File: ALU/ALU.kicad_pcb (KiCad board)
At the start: 4 copper layers, 100 x 100 mm, 78 parts, among them IC1 SN74AHCT16245DGGR, J1 Conn_01x06_Pin, J2 Conn_02x15_Odd_Even, J3 Conn_02x15_Odd_Even, J4 Conn_02x15_Odd_Even, J5 Conn_01x01_Pin, J6 Conn_01x01_Pin, J7 Conn_01x01_Pin, J8 Conn_01x01_Pin, J9 Conn_01x02, U1 74AHC1G08, U10 74HCT21, U11 74AHC1G32DBVR, U12 74AHCT1G02DBVR, U13 74AHCT1G08DBVR, U14 74AHCT1G08DBVR, U15 74AHC1G32DBVR, U16 74AHC1G32DBVR, U17 74AHC1G08, U18 SN74AHCT16374DGGR, U19 74AHCT1G08DBVR, U2 SN74AHCT16374DGGR, U20 74AHCT1G02DBVR, U21 74AHCT1G02DBVR, U3 74AHC1G04DBVR, U4 74LS181, U5 74LS181, U6 74AHCT1G08DBVR, U7 74HCT11, U8 74LS181, U9 74LS181

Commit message: Started GPU
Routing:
- net GND: track 156.3 -> 159.2 mm, vias 41 -> 47
- net /INA/DIN2: track 13.1 -> 13.8 mm
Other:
- outline, holes or cut-outs redrawn

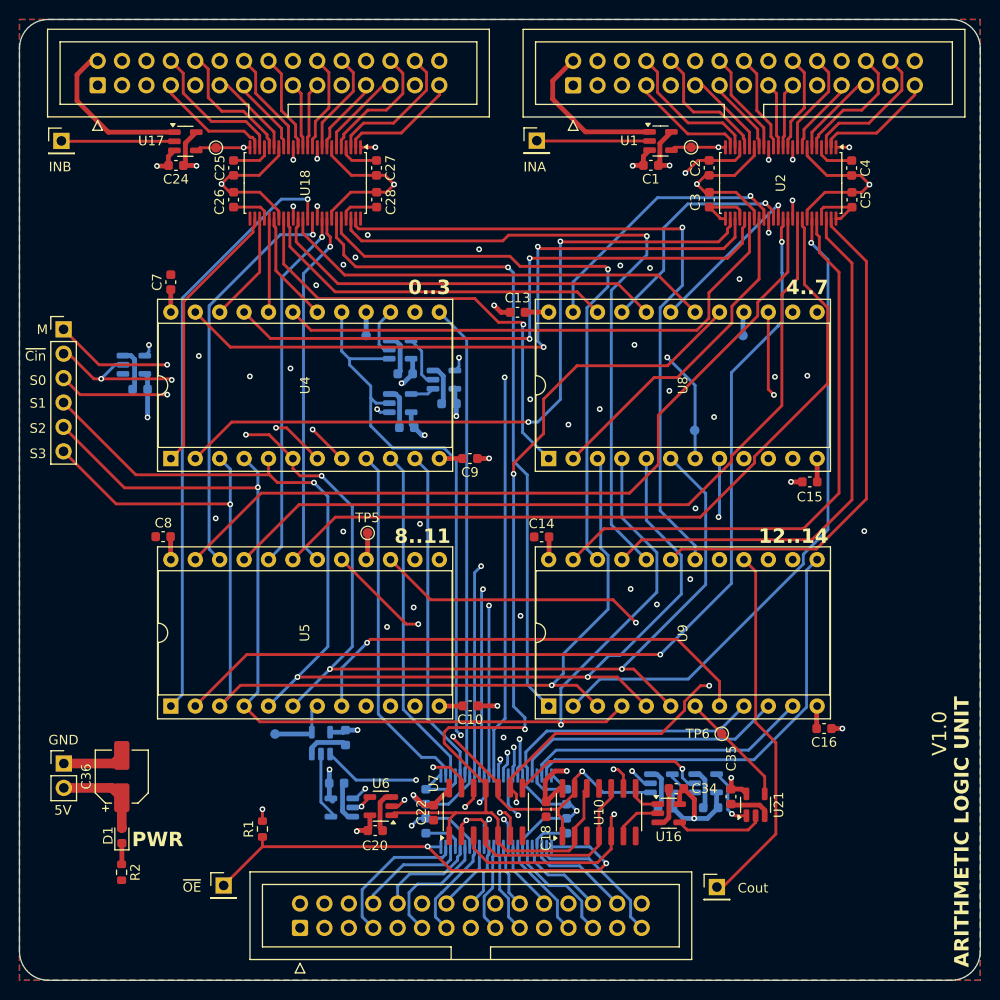
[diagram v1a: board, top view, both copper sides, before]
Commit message: Fixed incorrect wiring in ALU (input registers)
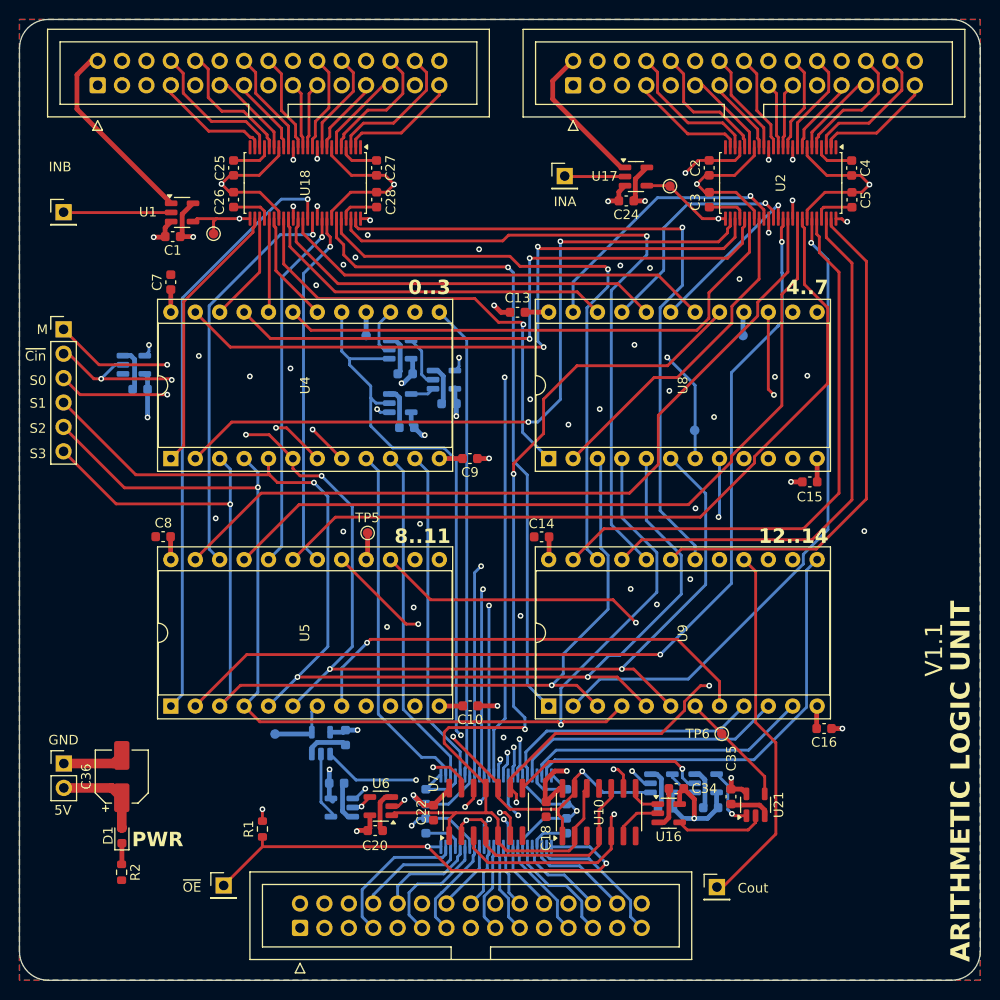
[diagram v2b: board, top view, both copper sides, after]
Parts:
- moved TP2 8.95 mm to (154.2, 36.3)
- moved J6 7.42 mm to (138.6, 34.1)
- moved C1 7.41 mm to (150.0, 36.6)
- moved U1 7.41 mm to (150.9, 34.1)
- moved J5 4.70 mm to (190.8, 30.3)
- moved TP1 4.61 mm to (201.7, 31.4)
- moved U17 4.50 mm to (198.2, 30.4)
- moved C24 4.50 mm to (197.2, 32.9)
- renumbered C24 to C1, C1 to C24, U17 to U1, U1 to U17
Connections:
- TP1 pad 1: Net-(U2-1~{OE}) -> Net-(U2-1CLK)
- TP2 pad 1: Net-(U18-1~{OE}) -> Net-(U18-1CLK)
- U1 pad 4: Net-(U18-1~{OE}) -> Net-(U18-1CLK)
- U17 pad 4: Net-(U2-1~{OE}) -> Net-(U2-1CLK)
- U18 pad 1: Net-(U18-1~{OE}) -> GND
- U18 pad 24: Net-(U18-1~{OE}) -> GND
- U18 pad 25: GND -> Net-(U18-1CLK)
- U18 pad 48: GND -> Net-(U18-1CLK)
- U2 pad 1: Net-(U2-1~{OE}) -> GND
- U2 pad 24: Net-(U2-1~{OE}) -> GND
- U2 pad 25: GND -> Net-(U2-1CLK)
- U2 pad 48: GND -> Net-(U2-1CLK)
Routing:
- net Net-(U2-1CLK): track 0.00 -> 24.4 mm, vias 0 -> 2
- net Net-(U18-1CLK): track 0.00 -> 22.4 mm, vias 0 -> 2
- net Net-(U18-1~{OE}): track 20.9 -> 0.00 mm, vias 2 -> 0
- net Net-(U2-1~{OE}): track 20.8 -> 0.00 mm, vias 2 -> 0
- net /INA: track 11.9 -> 6.30 mm
- net GND: track 159.2 -> 154.8 mm
- net /bus_connector2/CLK: track 17.0 -> 20.2 mm
- net /bus_connector/CLK: track 16.4 -> 15.3 mm
- net /INB: track 12.0 -> 11.3 mm
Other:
- board text added: "V1.1"
- board text removed: "V1.0"
